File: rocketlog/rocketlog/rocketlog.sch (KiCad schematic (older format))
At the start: 15 parts, among them J1 Conn_01x05_Female, U1 DSPIC33EP512GP502, U2 MCP2562, Y1 Crystal

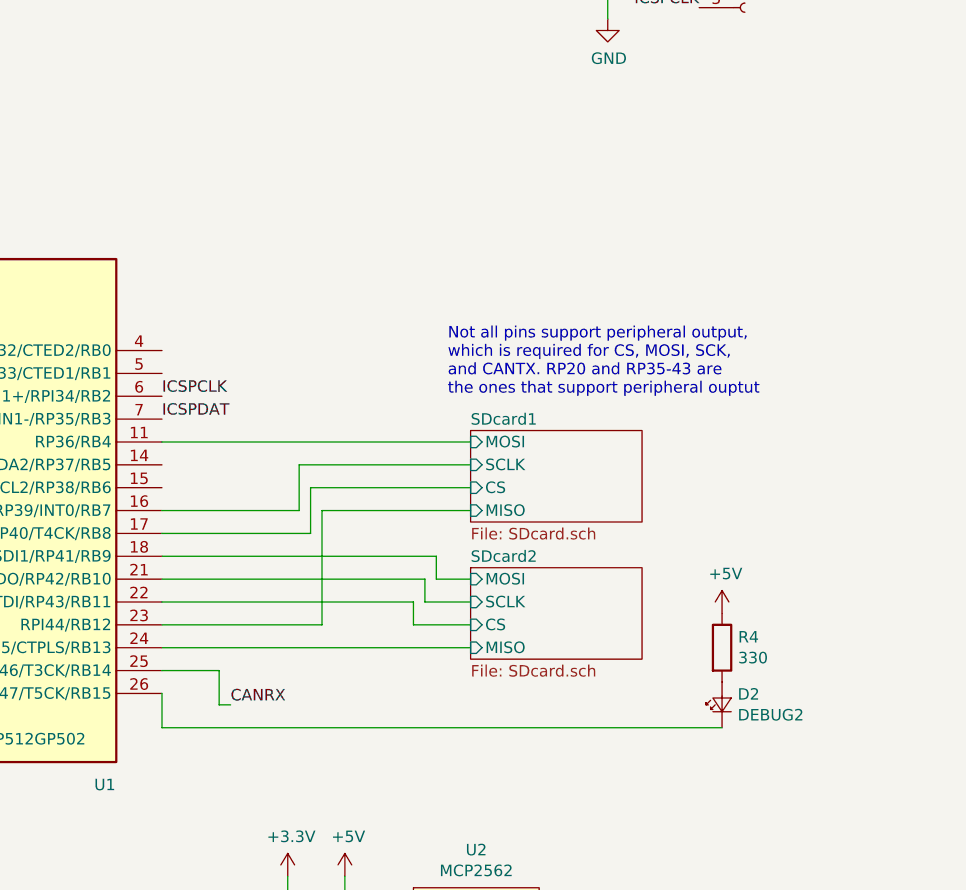
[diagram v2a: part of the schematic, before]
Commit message: Logger: route traces - got 95% of the way there
Required remapping a bunch of SD card pins. Only things that I
couldn't manage to route onto a 4cm by 6cm single sided board was the
current sense line, and a couple of ground pour islands. It should be
doable with maybe one or two jumpers. I want to try rotating the
microcontroller 90 degrees CCW, that should make the current sense
line easier, as well as some of the SD card stuff.
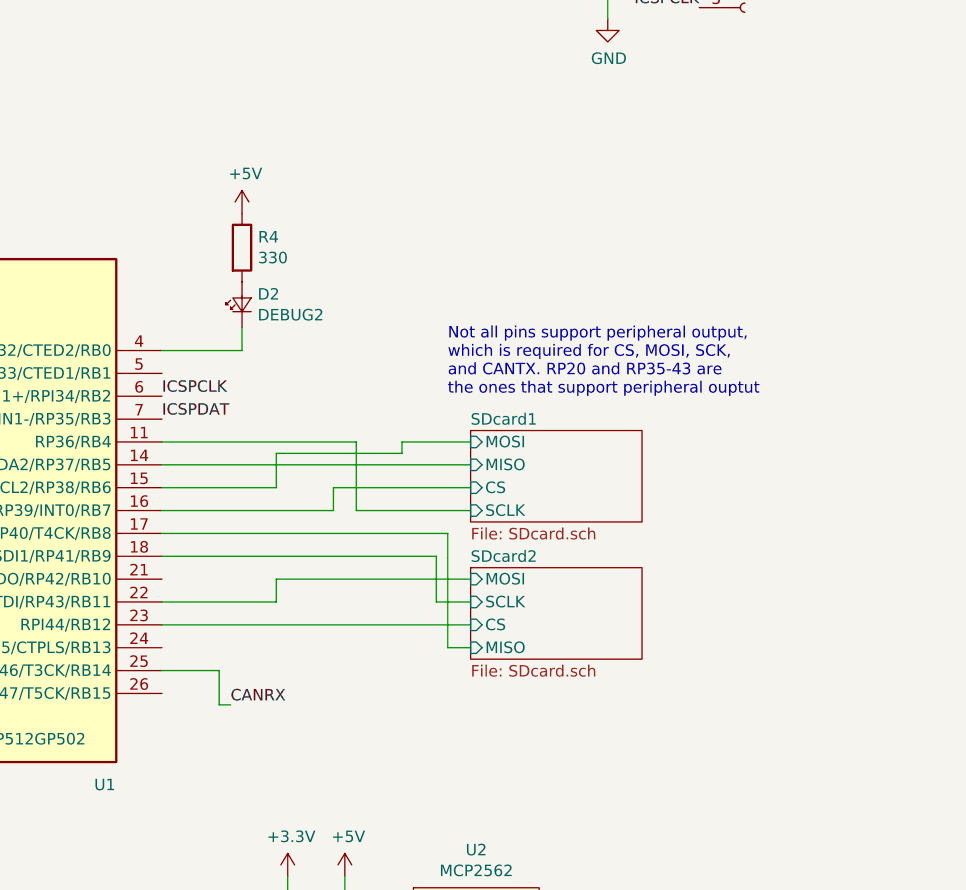
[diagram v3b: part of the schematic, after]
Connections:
- net SDcard1/CS: now also U1.16 (SCK1/RP39/INT0/RB7); no longer U1.17 (TCK/CVREF1O/ASCL1/SDO1/RP40/T4CK/RB8)
- net SDcard1/MISO: now also U1.14 (PGED2/ASDA2/RP37/RB5); no longer U1.23 (RPI44/RB12)
- net SDcard1/MOSI: now also U1.15 (PGEC2/ASCL2/RP38/RB6); no longer U1.11 (RP36/RB4)
- net SDcard1/SCLK: now also U1.11 (RP36/RB4); no longer U1.16 (SCK1/RP39/INT0/RB7)
- net SDcard2/CS: now also U1.23 (RPI44/RB12); no longer U1.22 (TDI/RP43/RB11)
- net SDcard2/MISO: now also U1.17 (TCK/CVREF1O/ASCL1/SDO1/RP40/T4CK/RB8); no longer U1.24 (RPI45/CTPLS/RB13)
- net SDcard2/MOSI: now also U1.22 (TDI/RP43/RB11); no longer U1.18 (TMS/ASDA1/SDI1/RP41/RB9)
- net SDcard2/SCLK: now also U1.18 (TMS/ASDA1/SDI1/RP41/RB9); no longer U1.21 (TDO/RP42/RB10)
- net at U1.26 (RPI47/T5CK/RB15): no longer D2.1 (K)
- net at U1.4 (PGED3/VREF-/AN2/C2IN1-/RPI32/CTED2/RB0): now also D2.1 (K)
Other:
- moved on the sheet: D2, R4
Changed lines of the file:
@@
 F0 "SDcard1" 50
 F1 "SDcard.sch" 50
-F2 "MISO" I L 8750 3950 50
+F2 "MISO" I L 8750 3750 50
 F3 "MOSI" I L 8750 3650 50
-F4 "SCLK" I L 8750 3750 50
+F4 "SCLK" I L 8750 3950 50
 F5 "CS" I L 8750 3850 50
 $EndSheet
@@
 Text Notes 8650 3450 0    50   ~ 0
 Not all pins support peripheral output,\nwhich is required for CS, MOSI, SCK,\nand CANTX. RP20 and RP35-43 are \nthe ones that support peripheral ouptut
-Wire Wire Line
-	7400 3650 8750 3650
-Wire Wire Line
-	7400 3950 8000 3950
-Wire Wire Line
-	8000 3950 8000 3750
-Wire Wire Line
-	8000 3750 8750 3750
-Wire Wire Line
-	7400 4050 8050 4050
-Wire Wire Line
-	8050 4050 8050 3850
-Wire Wire Line
-	8050 3850 8750 3850
-Wire Wire Line
-	7400 4150 8600 4150
-Wire Wire Line
-	8600 4150 8600 4250
-Wire Wire Line
-	8600 4250 8750 4250
-Wire Wire Line
-	7400 4250 8550 4250
-Wire Wire Line
-	8550 4250 8550 4350
-Wire Wire Line
-	8550 4350 8750 4350
-Wire Wire Line
-	7400 4350 8500 4350
-Wire Wire Line
-	8500 4350 8500 4450
-Wire Wire Line
-	8500 4450 8750 4450
-Wire Wire Line
-	8100 3950 8750 3950
-Wire Wire Line
-	7400 4550 8750 4550
 Text Label 3900 5050 2    50   ~ 0
 CANTX
@@
 L Device:LED_Small D2
 U 1 1 5B9F454C
-P 9850 4800
-F 0 "D2" V 9896 4732 50  0000 R CNN
-F 1 "DEBUG2" V 9805 4732 50  0000 R CNN
-F 2 "LED_SMD:LED_1206_3216Metric_Pad1.42x1.75mm_HandSolder" V 9850 4800 50  0001 C CNN
-F 3 "~" V 9850 4800 50  0001 C CNN
-	1    9850 4800
+P 7750 3050
+F 0 "D2" V 7796 2982 50  0000 R CNN
+F 1 "DEBUG2" V 7705 2982 50  0000 R CNN
+F 2 "LED_SMD:LED_1206_3216Metric_Pad1.42x1.75mm_HandSolder" V 7750 3050 50  0001 C CNN
+F 3 "~" V 7750 3050 50  0001 C CNN
+	1    7750 3050
 	0    -1   -1   0
 $EndComp
@@
 Wire Wire Line
 	3100 4300 3100 4450
-Wire Wire Line
-	3100 4450 4200 4450
 $Comp
 L power:+5V #PWR08
@@
 L power:+5V #PWR010
 U 1 1 5B9FF607
-P 9850 4400
-F 0 "#PWR010" H 9850 4250 50  0001 C CNN
-F 1 "+5V" H 9865 4573 50  0000 C CNN
-F 2 "" H 9850 4400 50  0001 C CNN
-F 3 "" H 9850 4400 50  0001 C CNN
-	1    9850 4400
-	1    0    0    -1
-$EndComp
-Wire Wire Line
-	7400 4750 7400 4900
-Wire Wire Line
-	7400 4900 9850 4900
-Wire Wire Line
-	7400 4450 8100 4450
-Wire Wire Line
-	8100 3950 8100 4450
+P 7750 2650
+F 0 "#PWR010" H 7750 2500 50  0001 C CNN
+F 1 "+5V" H 7765 2823 50  0000 C CNN
+F 2 "" H 7750 2650 50  0001 C CNN
+F 3 "" H 7750 2650 50  0001 C CNN
+	1    7750 2650
+	1    0    0    -1
+$EndComp
 Text GLabel 4200 4350 0    50   Input ~ 0
 CURR_AMP
@@
 L Device:R R4
 U 1 1 5BAC6DFE
-P 9850 4550
-F 0 "R4" H 9920 4596 50  0000 L CNN
-F 1 "330" H 9920 4505 50  0000 L CNN
-F 2 "Resistor_SMD:R_0805_2012Metric_Pad1.15x1.40mm_HandSolder" V 9780 4550 50  0001 C CNN
-F 3 "~" H 9850 4550 50  0001 C CNN
-	1    9850 4550
-	1    0    0    -1
-$EndComp
+P 7750 2800
+F 0 "R4" H 7820 2846 50  0000 L CNN
+F 1 "330" H 7820 2755 50  0000 L CNN
+F 2 "Resistor_SMD:R_0805_2012Metric_Pad1.15x1.40mm_HandSolder" V 7680 2800 50  0001 C CNN
+F 3 "~" H 7750 2800 50  0001 C CNN
+	1    7750 2800
+	1    0    0    -1
+$EndComp
+Wire Wire Line
+	7400 3750 8750 3750
+Wire Wire Line
+	7400 4050 8650 4050
+Wire Wire Line
+	7400 4150 8600 4150
+Wire Wire Line
+	8600 4150 8600 4350
+Wire Wire Line
+	8600 4350 8750 4350
+Wire Wire Line
+	8650 4550 8750 4550
+Wire Wire Line
+	8650 4050 8650 4550
+Wire Wire Line
+	7400 3950 8150 3950
+Wire Wire Line
+	8150 3950 8150 3850
+Wire Wire Line
+	8150 3850 8750 3850
+Wire Wire Line
+	7400 3650 8250 3650
+Wire Wire Line
+	8250 3650 8250 3950
+Wire Wire Line
+	8250 3950 8750 3950
+Wire Wire Line
+	7900 3850 7900 3700
+Wire Wire Line
+	7900 3700 8450 3700
+Wire Wire Line
+	8450 3700 8450 3650
+Wire Wire Line
+	8450 3650 8750 3650
+Wire Wire Line
+	7400 3850 7900 3850
+Wire Wire Line
+	3100 4450 4200 4450
+Wire Wire Line
+	7400 3250 7750 3250
+Wire Wire Line
+	7750 3250 7750 3150
+Wire Wire Line
+	7400 4450 8750 4450
+Wire Wire Line
+	7400 4350 7900 4350
+Wire Wire Line
+	7900 4350 7900 4250
+Wire Wire Line
+	7900 4250 8750 4250
 $EndSCHEMATC

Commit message: Logger: New layout, 5cm by 4.5cm. Not all connected.
Used one jumper, probably need 2 more to connect everything together
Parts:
- removed R2: 470, Resistor_SMD:R_0805_2012Metric_Pad1.15x1.40mm_HandSolder, symbol Device:R
- added JP1: Jumper_2_Bridged, canhw_footprints:Jumper_952-1474-2-ND, symbol Jumper:Jumper_2_Bridged
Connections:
- net labels added: SD1_CS, SD1_MISO, SD1_MOSI, SD1_SCLK, SD2_CS, SD2_MISO, SD2_MOSI, SD2_SCLK
- wire segments 74 -> 56
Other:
- note added: "Not all pins support peripheral output,\nwhich is required for MOSI, SCK,\nand CANTX. RP20 and RP35-43 are \nthe ones that support peripheral ouptut"
- note removed: "Not all pins support peripheral output,\nwhich is required for CS, MOSI, SCK,\nand CANTX. RP20 and RP35-43 are \nthe ones that support peripheral ouptut"
- moved on the sheet: D1, D2, R3, R4
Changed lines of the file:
@@
 Wire Wire Line
 	3950 3650 4200 3650
-$Comp
-L Device:R R2
-U 1 1 5B9D1F66
-P 3950 3250
-F 0 "R2" V 3800 3250 50  0000 C BNN
-F 1 "470" V 3850 3250 50  0000 C CNN
-F 2 "Resistor_SMD:R_0805_2012Metric_Pad1.15x1.40mm_HandSolder" V 3880 3250 50  0001 C CNN
-F 3 "~" H 3950 3250 50  0001 C CNN
-	1    3950 3250
-	0    1    -1   0
-$EndComp
-Wire Wire Line
-	3700 3250 3800 3250
 Connection ~ 3700 3250
-Wire Wire Line
-	4100 3250 4200 3250
 $Comp
 L power:GND #PWR011
@@
 	2300 5350 2300 5200
 $Sheet
-S 8750 3600 750  400
+S 9700 3600 750  400
 U 5B9D7D87
 F0 "SDcard1" 50
 F1 "SDcard.sch" 50
-F2 "MISO" I L 8750 3750 50
-F3 "MOSI" I L 8750 3650 50
-F4 "SCLK" I L 8750 3950 50
-F5 "CS" I L 8750 3850 50
+F2 "MISO" I L 9700 3750 50
+F3 "MOSI" I L 9700 3650 50
+F4 "SCLK" I L 9700 3950 50
+F5 "CS" I L 9700 3850 50
 $EndSheet
 $Sheet
-S 8750 4200 750  400
+S 9700 4150 750  400
 U 5B9D8C66
 F0 "SDcard2" 50
 F1 "SDcard.sch" 50
-F2 "MISO" I L 8750 4550 50
-F3 "MOSI" I L 8750 4250 50
-F4 "SCLK" I L 8750 4350 50
-F5 "CS" I L 8750 4450 50
+F2 "MISO" I L 9700 4500 50
+F3 "MOSI" I L 9700 4200 50
+F4 "SCLK" I L 9700 4300 50
+F5 "CS" I L 9700 4400 50
 $EndSheet
 Text Notes 8650 3450 0    50   ~ 0
-Not all pins support peripheral output,\nwhich is required for CS, MOSI, SCK,\nand CANTX. RP20 and RP35-43 are \nthe ones that support peripheral ouptut
-Text Label 3900 5050 2    50   ~ 0
-CANTX
-Text Label 7700 4800 0    50   ~ 0
+Not all pins support peripheral output,\nwhich is required for MOSI, SCK,\nand CANTX. RP20 and RP35-43 are \nthe ones that support peripheral ouptut
+Text Label 7400 4750 0    50   ~ 0
 CANRX
-Wire Wire Line
-	7400 4650 7650 4650
-Wire Wire Line
-	7650 4650 7650 4800
-Wire Wire Line
-	7650 4800 7700 4800
 Wire Wire Line
 	4200 5050 4200 4750
@@
 L Device:LED_Small D2
 U 1 1 5B9F454C
-P 7750 3050
-F 0 "D2" V 7796 2982 50  0000 R CNN
-F 1 "DEBUG2" V 7705 2982 50  0000 R CNN
-F 2 "LED_SMD:LED_1206_3216Metric_Pad1.42x1.75mm_HandSolder" V 7750 3050 50  0001 C CNN
-F 3 "~" V 7750 3050 50  0001 C CNN
-	1    7750 3050
+P 8050 4350
+F 0 "D2" V 8096 4282 50  0000 R CNN
+F 1 "DEBUG2" V 8005 4282 50  0000 R CNN
+F 2 "LED_SMD:LED_1206_3216Metric_Pad1.42x1.75mm_HandSolder" V 8050 4350 50  0001 C CNN
+F 3 "~" V 8050 4350 50  0001 C CNN
+	1    8050 4350
 	0    -1   -1   0
 $EndComp
@@
 L Device:LED_Small D1
 U 1 1 5B9F46EE
-P 3100 4200
-F 0 "D1" V 3150 4350 50  0000 R CNN
-F 1 "DEBUG1" V 3050 4550 50  0000 R CNN
-F 2 "LED_SMD:LED_1206_3216Metric_Pad1.42x1.75mm_HandSolder" V 3100 4200 50  0001 C CNN
-F 3 "~" V 3100 4200 50  0001 C CNN
-	1    3100 4200
+P 8650 4400
+F 0 "D1" V 8700 4550 50  0000 R CNN
+F 1 "DEBUG1" V 8600 4750 50  0000 R CNN
+F 2 "LED_SMD:LED_1206_3216Metric_Pad1.42x1.75mm_HandSolder" V 8650 4400 50  0001 C CNN
+F 3 "~" V 8650 4400 50  0001 C CNN
+	1    8650 4400
 	0    -1   -1   0
 $EndComp
@@
 Text Label 4200 4650 2    50   ~ 0
 OSC2
-Wire Wire Line
-	3100 4300 3100 4450
 $Comp
 L power:+5V #PWR08
 U 1 1 5B9FF5DB
-P 3100 3800
-F 0 "#PWR08" H 3100 3650 50  0001 C CNN
-F 1 "+5V" H 3115 3973 50  0000 C CNN
-F 2 "" H 3100 3800 50  0001 C CNN
-F 3 "" H 3100 3800 50  0001 C CNN
-	1    3100 3800
+P 8650 4000
+F 0 "#PWR08" H 8650 3850 50  0001 C CNN
+F 1 "+5V" H 8665 4173 50  0000 C CNN
+F 2 "" H 8650 4000 50  0001 C CNN
+F 3 "" H 8650 4000 50  0001 C CNN
+	1    8650 4000
 	1    0    0    -1
 $EndComp
@@
 L power:+5V #PWR010
 U 1 1 5B9FF607
-P 7750 2650
-F 0 "#PWR010" H 7750 2500 50  0001 C CNN
-F 1 "+5V" H 7765 2823 50  0000 C CNN
-F 2 "" H 7750 2650 50  0001 C CNN
-F 3 "" H 7750 2650 50  0001 C CNN
-	1    7750 2650
-	1    0    0    -1
-$EndComp
-Text GLabel 4200 4350 0    50   Input ~ 0
+P 8050 3950
+F 0 "#PWR010" H 8050 3800 50  0001 C CNN
+F 1 "+5V" H 8065 4123 50  0000 C CNN
+F 2 "" H 8050 3950 50  0001 C CNN
+F 3 "" H 8050 3950 50  0001 C CNN
+	1    8050 3950
+	1    0    0    -1
+$EndComp
+Text GLabel 3300 4450 0    50   Input ~ 0
 CURR_AMP
 $Sheet
@@
 L Device:R R3
 U 1 1 5BAC6D7D
-P 3100 3950
-F 0 "R3" H 3170 3996 50  0000 L CNN
-F 1 "330" H 3170 3905 50  0000 L CNN
-F 2 "Resistor_SMD:R_0805_2012Metric_Pad1.15x1.40mm_HandSolder" V 3030 3950 50  0001 C CNN
-F 3 "~" H 3100 3950 50  0001 C CNN
-	1    3100 3950
+P 8650 4150
+F 0 "R3" H 8720 4196 50  0000 L CNN
+F 1 "330" H 8720 4105 50  0000 L CNN
+F 2 "Resistor_SMD:R_0805_2012Metric_Pad1.15x1.40mm_HandSolder" V 8580 4150 50  0001 C CNN
+F 3 "~" H 8650 4150 50  0001 C CNN
+	1    8650 4150
 	1    0    0    -1
 $EndComp
@@
 L Device:R R4
 U 1 1 5BAC6DFE
-P 7750 2800
-F 0 "R4" H 7820 2846 50  0000 L CNN
-F 1 "330" H 7820 2755 50  0000 L CNN
-F 2 "Resistor_SMD:R_0805_2012Metric_Pad1.15x1.40mm_HandSolder" V 7680 2800 50  0001 C CNN
-F 3 "~" H 7750 2800 50  0001 C CNN
-	1    7750 2800
-	1    0    0    -1
-$EndComp
-Wire Wire Line
-	7400 3750 8750 3750
-Wire Wire Line
-	7400 4050 8650 4050
-Wire Wire Line
-	7400 4150 8600 4150
-Wire Wire Line
-	8600 4150 8600 4350
-Wire Wire Line
-	8600 4350 8750 4350
-Wire Wire Line
-	8650 4550 8750 4550
-Wire Wire Line
-	8650 4050 8650 4550
-Wire Wire Line
-	7400 3950 8150 3950
-Wire Wire Line
-	8150 3950 8150 3850
-Wire Wire Line
-	8150 3850 8750 3850
-Wire Wire Line
-	7400 3650 8250 3650
-Wire Wire Line
-	8250 3650 8250 3950
-Wire Wire Line
-	8250 3950 8750 3950
-Wire Wire Line
-	7900 3850 7900 3700
-Wire Wire Line
-	7900 3700 8450 3700
-Wire Wire Line
-	8450 3700 8450 3650
-Wire Wire Line
-	8450 3650 8750 3650
-Wire Wire Line
-	7400 3850 7900 3850
-Wire Wire Line
-	3100 4450 4200 4450
-Wire Wire Line
-	7400 3250 7750 3250
-Wire Wire Line
-	7750 3250 7750 3150
-Wire Wire Line
-	7400 4450 8750 4450
-Wire Wire Line
-	7400 4350 7900 4350
-Wire Wire Line
-	7900 4350 7900 4250
-Wire Wire Line
-	7900 4250 8750 4250
+P 8050 4100
+F 0 "R4" H 8120 4146 50  0000 L CNN
+F 1 "330" H 8120 4055 50  0000 L CNN
+F 2 "Resistor_SMD:R_0805_2012Metric_Pad1.15x1.40mm_HandSolder" V 7980 4100 50  0001 C CNN
+F 3 "~" H 8050 4100 50  0001 C CNN
+	1    8050 4100
+	1    0    0    -1
+$EndComp
+Wire Wire Line
+	3700 3250 4200 3250
+Text Label 9550 3650 2    50   ~ 0
+SD1_MOSI
+Text Label 9550 3750 2    50   ~ 0
+SD1_MISO
+Text Label 9550 3850 2    50   ~ 0
+SD1_CS
+Text Label 9550 3950 2    50   ~ 0
+SD1_SCLK
+Wire Wire Line
+	9550 3950 9700 3950
+Wire Wire Line
+	9550 3850 9700 3850
+Wire Wire Line
+	9550 3750 9700 3750
+Wire Wire Line
+	9550 3650 9700 3650
+Text Label 9550 4200 2    50   ~ 0
+SD2_MOSI
+Text Label 9550 4300 2    50   ~ 0
+SD2_MISO
+Text Label 9550 4400 2    50   ~ 0
+SD2_CS
+Text Label 9550 4500 2    50   ~ 0
+SD2_SCLK
+Wire Wire Line
+	9550 4500 9700 4500
+Wire Wire Line
+	9550 4400 9700 4400
+Wire Wire Line
+	9550 4300 9700 4300
+Wire Wire Line
+	9550 4200 9700 4200
+Text Label 4200 4350 2    50   ~ 0
+SD1_CS
+Text Label 7400 3650 0    50   ~ 0
+SD1_MOSI
+Text Label 7400 3750 0    50   ~ 0
+SD1_MISO
+Text Label 3900 5050 2    50   ~ 0
+SD1_SCLK
+Text Label 7400 4150 0    50   ~ 0
+SD2_MOSI
+Text Label 7400 4250 0    50   ~ 0
+SD2_MISO
+Text Label 7400 4050 0    50   ~ 0
+SD2_CS
+Text Label 7400 4350 0    50   ~ 0
+SD2_SCLK
+Text Label 7400 3850 0    50   ~ 0
+CANTX
+Wire Wire Line
+	7400 4450 8050 4450
+Wire Wire Line
+	8650 4500 8650 4550
+Wire Wire Line
+	8650 4550 7400 4550
+$Comp
+L Jumper:Jumper_2_Bridged JP1
+U 1 1 5BB0EE30
+P 3500 4450
+F 0 "JP1" H 3500 4645 50  0000 C CNN
+F 1 "Jumper_2_Bridged" H 3500 4554 50  0000 C CNN
+F 2 "canhw_footprints:Jumper_952-1474-2-ND" H 3500 4450 50  0001 C CNN
+F 3 "~" H 3500 4450 50  0001 C CNN
+	1    3500 4450
+	1    0    0    -1
+$EndComp
+Wire Wire Line
+	3700 4450 4200 4450
 $EndSCHEMATC

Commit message: Logger: A final, working layout of single layer board. Needs tweaking.
All nets are connected, it fits on a 4.5x5cm pcb, some parts need to
be moved around slightly so I don't hate myself when assembling. I
think that this is the one to go with. After some tweaking.
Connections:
- wire segments 56 -> 57
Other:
- moved on the sheet: D2
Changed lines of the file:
@@
 Text Notes 8650 3450 0    50   ~ 0
 Not all pins support peripheral output,\nwhich is required for MOSI, SCK,\nand CANTX. RP20 and RP35-43 are \nthe ones that support peripheral ouptut
-Text Label 7400 4750 0    50   ~ 0
+Text Label 7400 4250 0    50   ~ 0
 CANRX
 Wire Wire Line
@@
 F 3 "~" V 8050 4350 50  0001 C CNN
 	1    8050 4350
-	0    -1   -1   0
+	0    1    -1   0
 $EndComp
 $Comp
@@
 	1    0    0    -1
 $EndComp
-Text GLabel 3300 4450 0    50   Input ~ 0
+Text GLabel 3700 4450 0    50   Input ~ 0
 CURR_AMP
 $Sheet
@@
 Wire Wire Line
 	9550 4200 9700 4200
-Text Label 4200 4350 2    50   ~ 0
+Text Label 7400 4150 0    50   ~ 0
 SD1_CS
+Text Label 7400 4050 0    50   ~ 0
+SD1_MOSI
+Text Label 7400 3850 0    50   ~ 0
+SD1_MISO
+Text Label 7400 3950 0    50   ~ 0
+SD1_SCLK
 Text Label 7400 3650 0    50   ~ 0
-SD1_MOSI
+SD2_MOSI
+Text Label 3900 5050 2    50   ~ 0
+SD2_MISO
+Text Label 7400 3250 0    50   ~ 0
+SD2_CS
 Text Label 7400 3750 0    50   ~ 0
-SD1_MISO
-Text Label 3900 5050 2    50   ~ 0
-SD1_SCLK
-Text Label 7400 4150 0    50   ~ 0
-SD2_MOSI
-Text Label 7400 4250 0    50   ~ 0
-SD2_MISO
-Text Label 7400 4050 0    50   ~ 0
-SD2_CS
+SD2_SCLK
 Text Label 7400 4350 0    50   ~ 0
-SD2_SCLK
-Text Label 7400 3850 0    50   ~ 0
 CANTX
-Wire Wire Line
-	7400 4450 8050 4450
 Wire Wire Line
 	8650 4500 8650 4550
@@
 L Jumper:Jumper_2_Bridged JP1
 U 1 1 5BB0EE30
-P 3500 4450
-F 0 "JP1" H 3500 4645 50  0000 C CNN
-F 1 "Jumper_2_Bridged" H 3500 4554 50  0000 C CNN
-F 2 "canhw_footprints:Jumper_952-1474-2-ND" H 3500 4450 50  0001 C CNN
-F 3 "~" H 3500 4450 50  0001 C CNN
-	1    3500 4450
-	1    0    0    -1
+P 1150 4250
+F 0 "JP1" H 1150 4445 50  0000 C CNN
+F 1 "Jumper_2_Bridged" H 1150 4354 50  0000 C CNN
+F 2 "canhw_footprints:Jumper_952-1474-2-ND" H 1150 4250 50  0001 C CNN
+F 3 "~" H 1150 4250 50  0001 C CNN
+	1    1150 4250
+	1    0    0    1
 $EndComp
 Wire Wire Line
 	3700 4450 4200 4450
+Wire Wire Line
+	8050 4450 8050 4650
+Wire Wire Line
+	8050 4650 7400 4650
 $EndSCHEMATC

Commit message: Logger Board PCB Review 1 changes
Changes in this commit:
        - Move C2 further from U1
        - Space out F1, R5, U4 and C8
        - Silkscreen rearrangements to make it pretty
        - Replace J1 (SMT programming header) with a 90 degree connector
        - Replace U3 with hand soldering footprints
        - Turn mounting holes into plated holes
        - Remove daisy chaining through pads. I hope I got all of them, please check
        - Get rid of the power trace running through the SD card housing....
        - Move SD card holders down, so the SD cards don't overhand the board
        - Add rocketry logo to front silkscreen for that sweet sweet brand value
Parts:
- removed JP1: Jumper_2_Bridged, canhw_footprints:Jumper_952-1474-2-ND, symbol Jumper:Jumper_2_Bridged
- J1: footprint Connector_PinHeader_2.54mm:PinHeader_1x05_P2.54mm_Vertical_SMD_Pin1Right -> canhw_footprints:PinHeader_5x2.54_SMD_90deg_952-3198-1-ND
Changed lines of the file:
@@
 F 0 "J1" H 9977 1576 50  0000 L CNN
 F 1 "Conn_01x05_Female" H 9977 1485 50  0000 L CNN
-F 2 "Connector_PinHeader_2.54mm:PinHeader_1x05_P2.54mm_Vertical_SMD_Pin1Right" H 9950 1550 50  0001 C CNN
+F 2 "canhw_footprints:PinHeader_5x2.54_SMD_90deg_952-3198-1-ND" H 9950 1550 50  0001 C CNN
 F 3 "~" H 9950 1550 50  0001 C CNN
 	1    9950 1550
-	1    0    0    -1
+	1    0    0    1
 $EndComp
 Text Label 9750 1350 2    50   ~ 0
@@
 Wire Wire Line
 	8650 4550 7400 4550
-$Comp
-L Jumper:Jumper_2_Bridged JP1
-U 1 1 5BB0EE30
-P 1150 4250
-F 0 "JP1" H 1150 4445 50  0000 C CNN
-F 1 "Jumper_2_Bridged" H 1150 4354 50  0000 C CNN
-F 2 "canhw_footprints:Jumper_952-1474-2-ND" H 1150 4250 50  0001 C CNN
-F 3 "~" H 1150 4250 50  0001 C CNN
-	1    1150 4250
-	1    0    0    1
-$EndComp
 Wire Wire Line
 	3700 4450 4200 4450
